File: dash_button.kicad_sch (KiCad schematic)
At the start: 60 parts, among them J1 MINI 5PTP, J2 1050570001, J3 Debug, J4 JST PH 1x2, J5 JST PH 1x5, P1 CONN_02X03, Q1 AO3401A, Q2 AO3401A, Q3 AO3401A, Q4 AO3401A, Q6 AO3401A, Q7 AO3400A, SW1 SW_Push, SW2 SW_Push, SW3 SW_Push, SW4 SW_Push, SW5 SW_Push, U1 ATtiny441-M, U2 HT7550-1

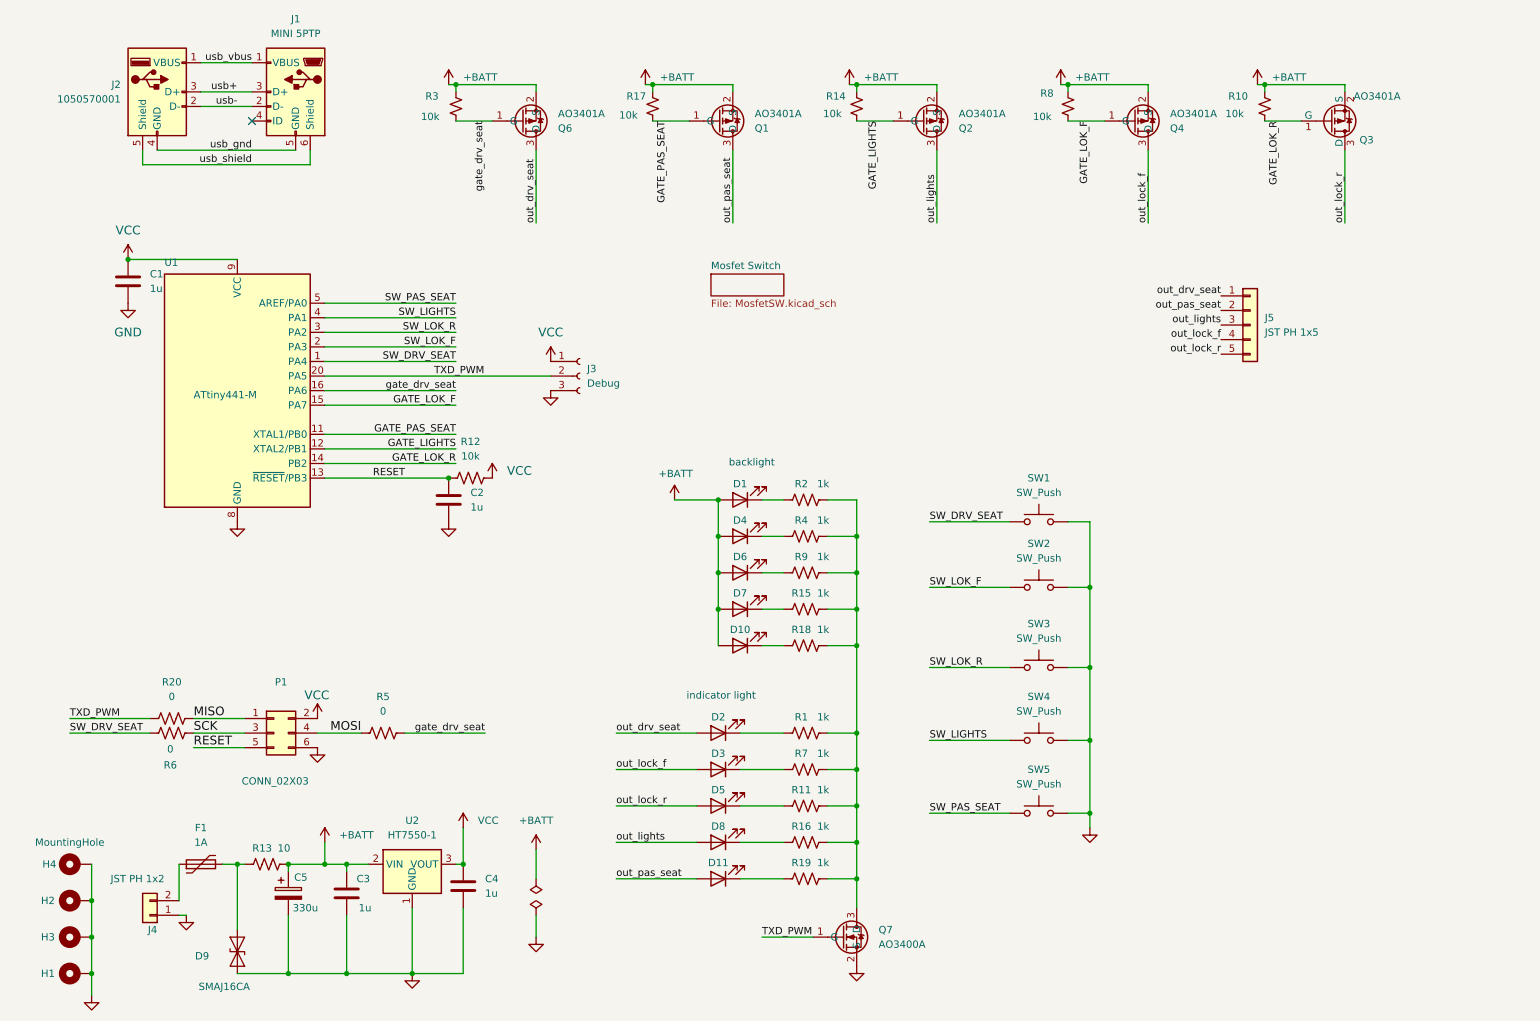
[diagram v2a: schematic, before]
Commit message: Move JST connectors to center
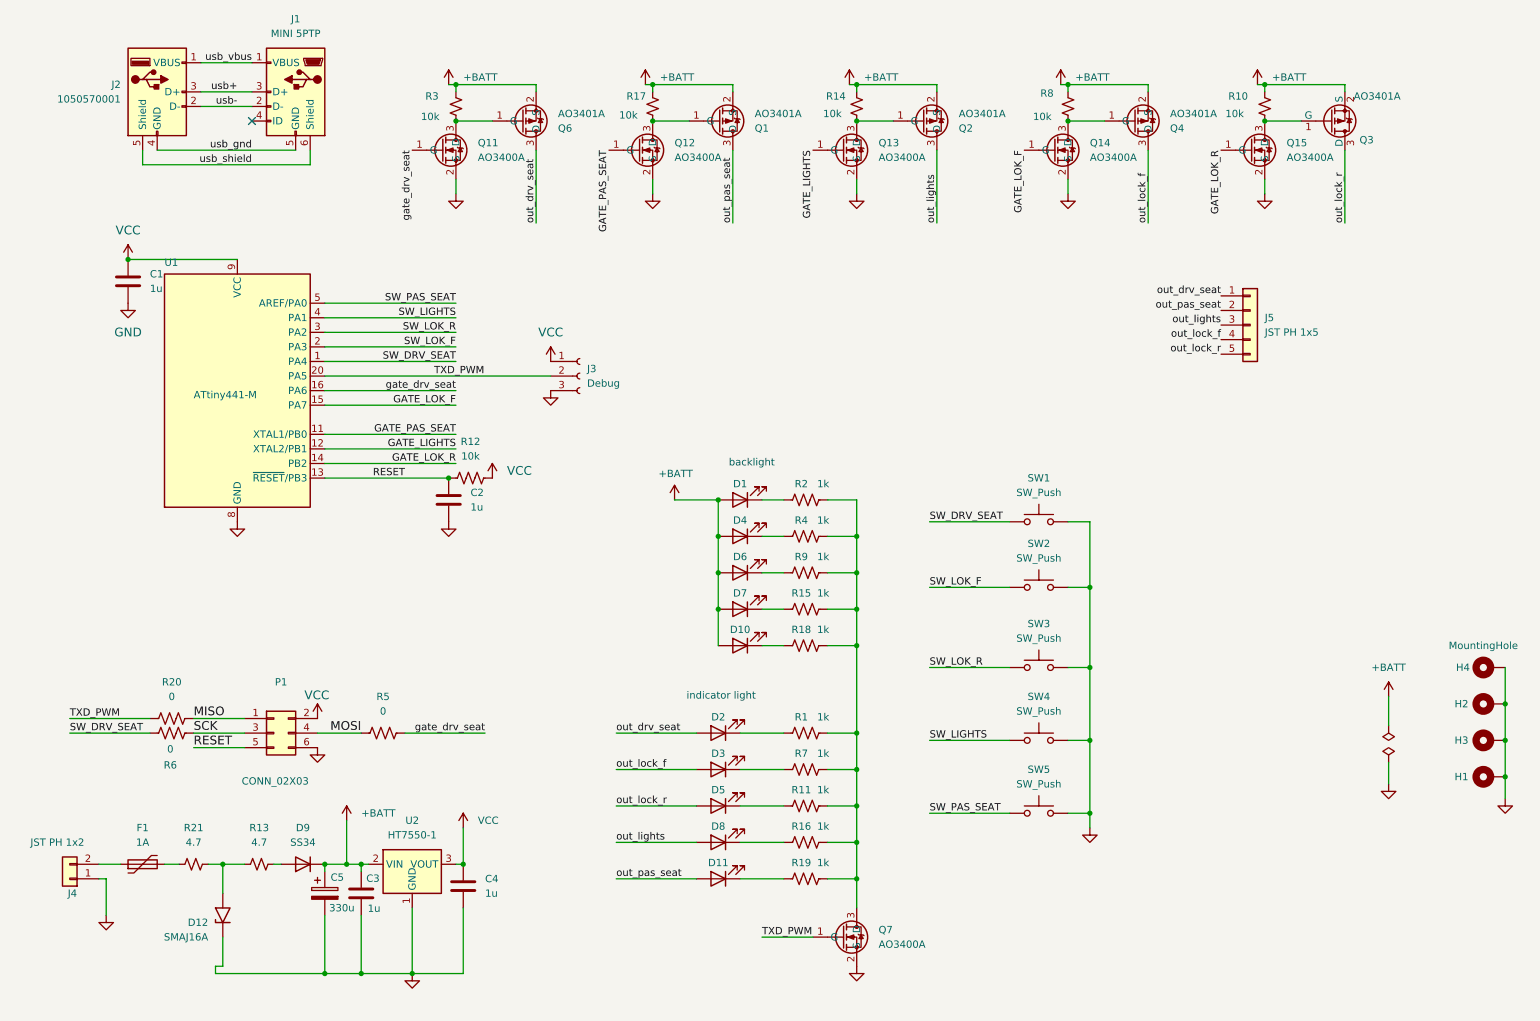
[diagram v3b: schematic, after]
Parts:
- removed D9: SMAJ16CA, Diode_SMD:D_SMA, symbol Diode:SMAJ20CA
- removed R13: 10, Resistor_SMD:R_0805_2012Metric_Pad1.20x1.40mm_HandSolder, symbol Device:R_US
- added D12: SMAJ16A, Diode_SMD:D_SMA, symbol Diode:SMAJ16A
- added D9: SS34, Diode_SMD:D_SMA, symbol Device:D
- added Q11, Q12, Q13, Q14, Q15: AO3400A, Package_TO_SOT_SMD:SOT-23, symbol Transistor_FET:AO3400A
- added R13, R21: 4.7, Resistor_SMD:R_0805_2012Metric_Pad1.20x1.40mm_HandSolder, symbol Device:R_Small_US
- P1: footprint project:programmer-pads -> Connector_PinHeader_2.54mm:PinHeader_2x03_P2.54mm_Vertical
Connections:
- net +BATT: now also D9.1 (K)
- net GATE_LIGHTS: now also Q13.1 (G); no longer Q2.1 (G), R14.2
- net GATE_LOK_F: now also Q14.1 (G); no longer Q4.1 (G), R8.2
- net GATE_LOK_R: now also Q15.1 (G); no longer Q3.1 (G), R10.2
- net GATE_PAS_SEAT: now also Q12.1 (G); no longer Q1.1 (G), R17.2
- net GND: now also D12.1 (A1), Q11.2 (S), Q12.2 (S), Q13.2 (S), Q14.2 (S), Q15.2 (S)
- net gate_drv_seat: now also Q11.1 (G); no longer Q6.1 (G), R3.2
- net at F1.2: now also R21.1
- new net: D9.2 (A), R13.2
- new net: Q14.3 (D), Q4.1 (G), R8.2
- new net: Q13.3 (D), Q2.1 (G), R14.2
- new net: D12.2 (A2), R13.1, R21.2
- new net: Q1.1 (G), Q12.3 (D), R17.2
- new net: Q11.3 (D), Q6.1 (G), R3.2
- new net: Q15.3 (D), Q3.1 (G), R10.2
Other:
- removed sheet Mosfet Switch
- moved on the sheet: C3, C5, F1, H1, H2, H3, H4, J4

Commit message: fixup BOM
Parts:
- C1, C2, C3, C4: MPN (none) -> CL10A105KB8NNNC
- C5: value 330u -> 100u; MPN (none) -> VES101M1CTR-0605; Manufacturer (none) -> Lelon
- D1, D10, D4, D6, D7: Manufacturer Hubei KENTO Elec -> Hubei KENTO Elec
- F1: MPN BSMD1206-100-30V -> BSMD1206-100-30V
- J3: MPN (none) -> ZX-PZ2.54-1-3PWZ; Manufacturer (none) -> Megastar
- P1: MPN (none) -> ZX-PZ2.54-2-3PZZ; Manufacturer (none) -> Megastar
- Q11, Q12, Q13, Q14, Q15: LCSC Part # (none) -> C20917; MPN (none) -> AO3400A; Manufacturer (none) -> Alpha & Omega Semicon
- SW1, SW2, SW3, SW4, SW5: value SW_Push -> TS-1002S-08526C; MPN TS-1002S-08526C -> TS-1002S-08526C

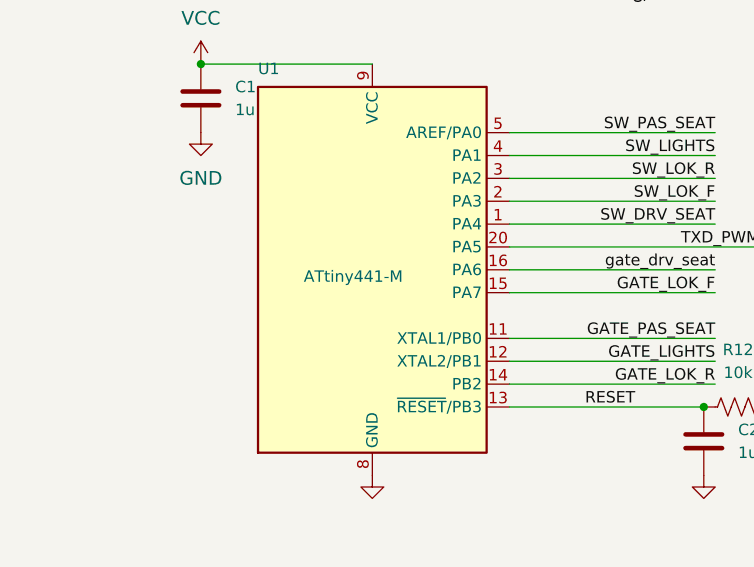
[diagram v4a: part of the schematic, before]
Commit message: Change Attiny part number to attiny441-mur
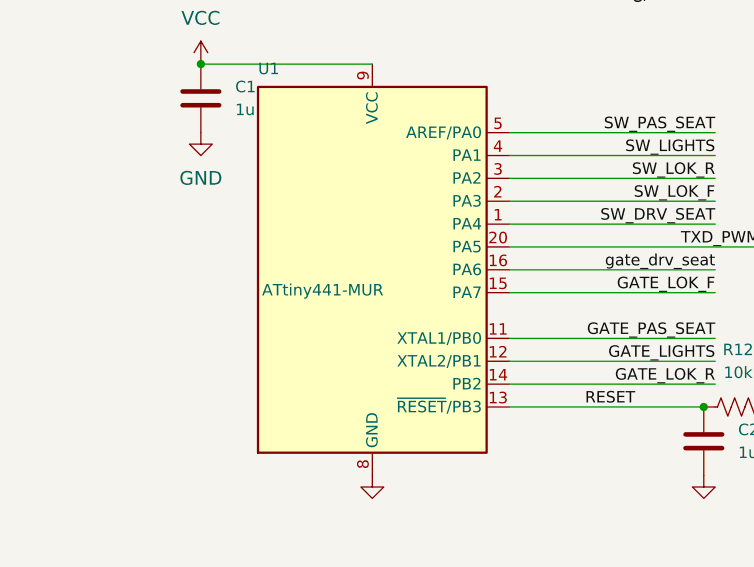
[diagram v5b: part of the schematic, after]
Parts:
- U1: value ATtiny441-M -> ATtiny441-MUR; MPN ATTINY441-MMH -> ATTINY441-MUR; PartNo ATTINY441-MUR -> (none)
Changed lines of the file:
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@@
 			)
 		)
-		(property "Value" "ATtiny441-M"
-			(at 46.99 85.09 0)
+		(property "Value" "ATtiny441-MUR"
+			(at 42.3559 86.6051 0)
 			(effects
 				(font
@@
 			)
 		)
-		(property "PartNo" "ATTINY441-MUR"
-			(at 54.61 85.09 0)
-			(effects
-				(font
-					(size 1.524 1.524)
-				)
-				(hide yes)
-			)
-		)
 		(property "Manufacturer" "ATMEL"
 			(at 54.61 85.09 0)
@@
 			)
 		)
-		(property "MPN" "ATTINY441-MMH"
+		(property "MPN" "ATTINY441-MUR"
 			(at 54.61 85.09 0)
 			(effects

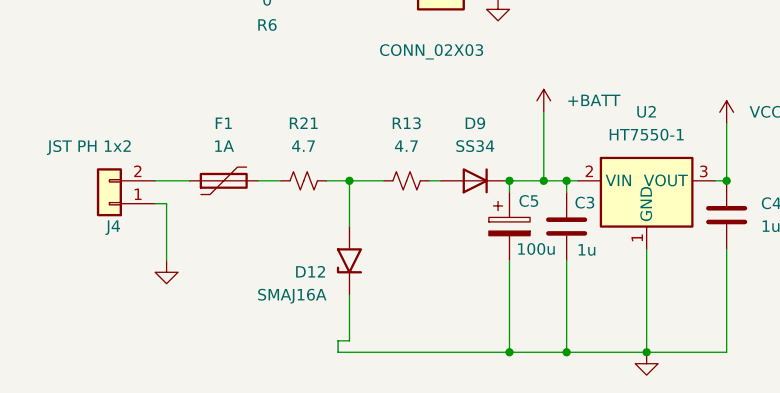
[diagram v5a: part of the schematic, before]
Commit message: flip around TVS Diode
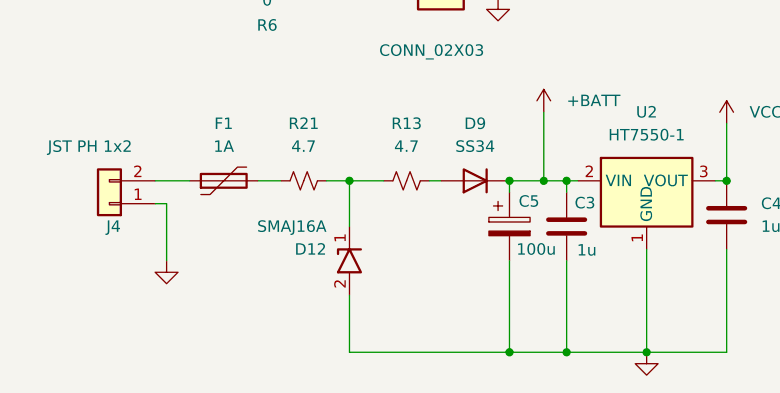
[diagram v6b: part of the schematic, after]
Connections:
- net GND: now also D12.2 (A2); no longer D12.1 (A1)
- net at R13.1, R21.2: now also D12.1 (A1); no longer D12.2 (A2)
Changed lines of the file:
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@@
 	(wire
 		(pts
-			(xy 50.8 185.42) (xy 52.07 185.42)
-		)
-		(stroke
-			(width 0)
-			(type default)
-		)
-	)
-	(wire
-		(pts
 			(xy 162.56 170.18) (xy 162.56 175.26)
 		)
@@
 	(wire
 		(pts
-			(xy 52.07 185.42) (xy 52.07 180.34)
+			(xy 52.07 180.34) (xy 52.07 186.69)
 		)
 		(stroke
@@
 	(wire
 		(pts
-			(xy 50.8 185.42) (xy 50.8 186.69)
-		)
-		(stroke
-			(width 0)
-			(type default)
-		)
-	)
-	(wire
-		(pts
 			(xy 142.24 170.18) (xy 149.86 170.18)
 		)
@@
 	(wire
 		(pts
-			(xy 50.8 186.69) (xy 69.85 186.69)
+			(xy 52.07 186.69) (xy 69.85 186.69)
 		)
 		(stroke
@@
 		(lib_id "Diode:SMAJ16A")
 		(at 52.07 176.53 90)
+		(mirror x)
 		(unit 1)
 		(exclude_from_sim no)
@@
 		(dnp no)
 		(property "Reference" "D12"
-			(at 49.53 177.8001 90)
+			(at 49.53 175.2599 90)
 			(effects
 				(font
@@
 		)
 		(property "Value" "SMAJ16A"
-			(at 49.53 180.34 90)
+			(at 49.53 172.72 90)
 			(effects
 				(font
@@
 		)
 		(property "Datasheet" "https://www.littelfuse.com/media?resourcetype=datasheets&itemid=75e32973-b177-4ee3-a0ff-cedaf1abdb93&filename=smaj-datasheet"
-			(at 52.07 177.8 0)
+			(at 52.07 175.26 0)
 			(effects
 				(font
